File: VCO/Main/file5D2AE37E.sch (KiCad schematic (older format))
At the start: 28 parts, among them U5 LM13700, U6 TL072, U7 TL072

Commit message: Resolve most of the issues in known_issues.txt
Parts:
- R25: value 10K -> 20K
- R35: value 20K -> 10K
- R38: value 24K -> 12K
- R39: value 9.1K -> 10K
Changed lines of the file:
@@
 EESchema Schematic File Version 4
-LIBS:AS3340_VCO-cache
-EELAYER 29 0
+LIBS:VCO_Main-cache
+EELAYER 30 0
 EELAYER END
 $Descr A4 11693 8268
@@
 AR Path="/5D2AE37F/5D4E2D40" Ref="R35"  Part="1"
 F 0 "R35" V 2105 6750 50  0000 C CNN
-F 1 "20K" V 2014 6750 50  0000 C CNN
+F 1 "10K" V 2014 6750 50  0000 C CNN
 F 2 "Resistor_SMD:R_0805_2012Metric" V 1940 6740 50  0001 C CNN
 F 3 "~" H 1900 6750 50  0001 C CNN
@@
 AR Path="/5D2AE37F/5D513054" Ref="R38"  Part="1"
 F 0 "R38" V 8355 5800 50  0000 C CNN
-F 1 "24K" V 8264 5800 50  0000 C CNN
+F 1 "12K" V 8264 5800 50  0000 C CNN
 F 2 "Resistor_SMD:R_0805_2012Metric" V 8190 5790 50  0001 C CNN
 F 3 "~" H 8150 5800 50  0001 C CNN
@@
 AR Path="/5D2AE37F/5D513604" Ref="R39"  Part="1"
 F 0 "R39" V 9155 6200 50  0000 C CNN
-F 1 "9.1K" V 9064 6200 50  0000 C CNN
+F 1 "10K" V 9064 6200 50  0000 C CNN
 F 2 "Resistor_SMD:R_0805_2012Metric" V 8990 6190 50  0001 C CNN
 F 3 "~" H 8950 6200 50  0001 C CNN
@@
 AR Path="/5D2AE37F/5D551AEB" Ref="R25"  Part="1"
 F 0 "R25" V 3255 4300 50  0000 C CNN
-F 1 "10K" V 3164 4300 50  0000 C CNN
+F 1 "20K" V 3164 4300 50  0000 C CNN
 F 2 "Resistor_SMD:R_0805_2012Metric" V 3090 4290 50  0001 C CNN
 F 3 "~" H 3050 4300 50  0001 C CNN

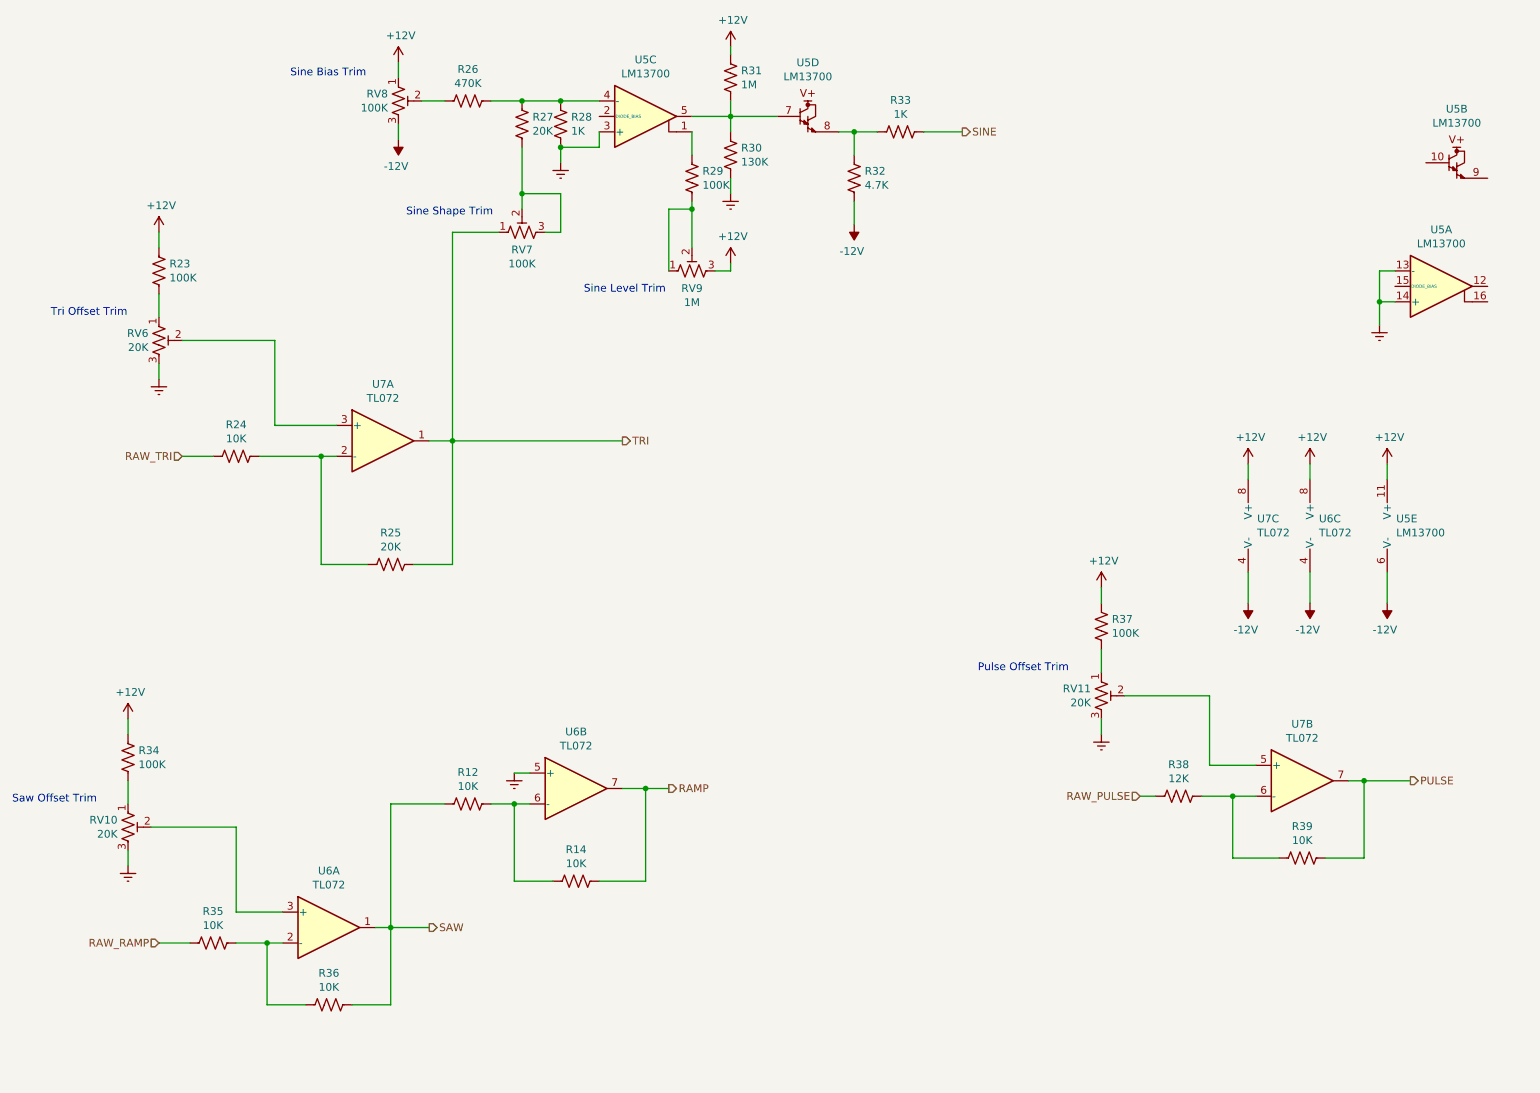
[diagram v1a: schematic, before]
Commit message: Clean up layout of VCO board
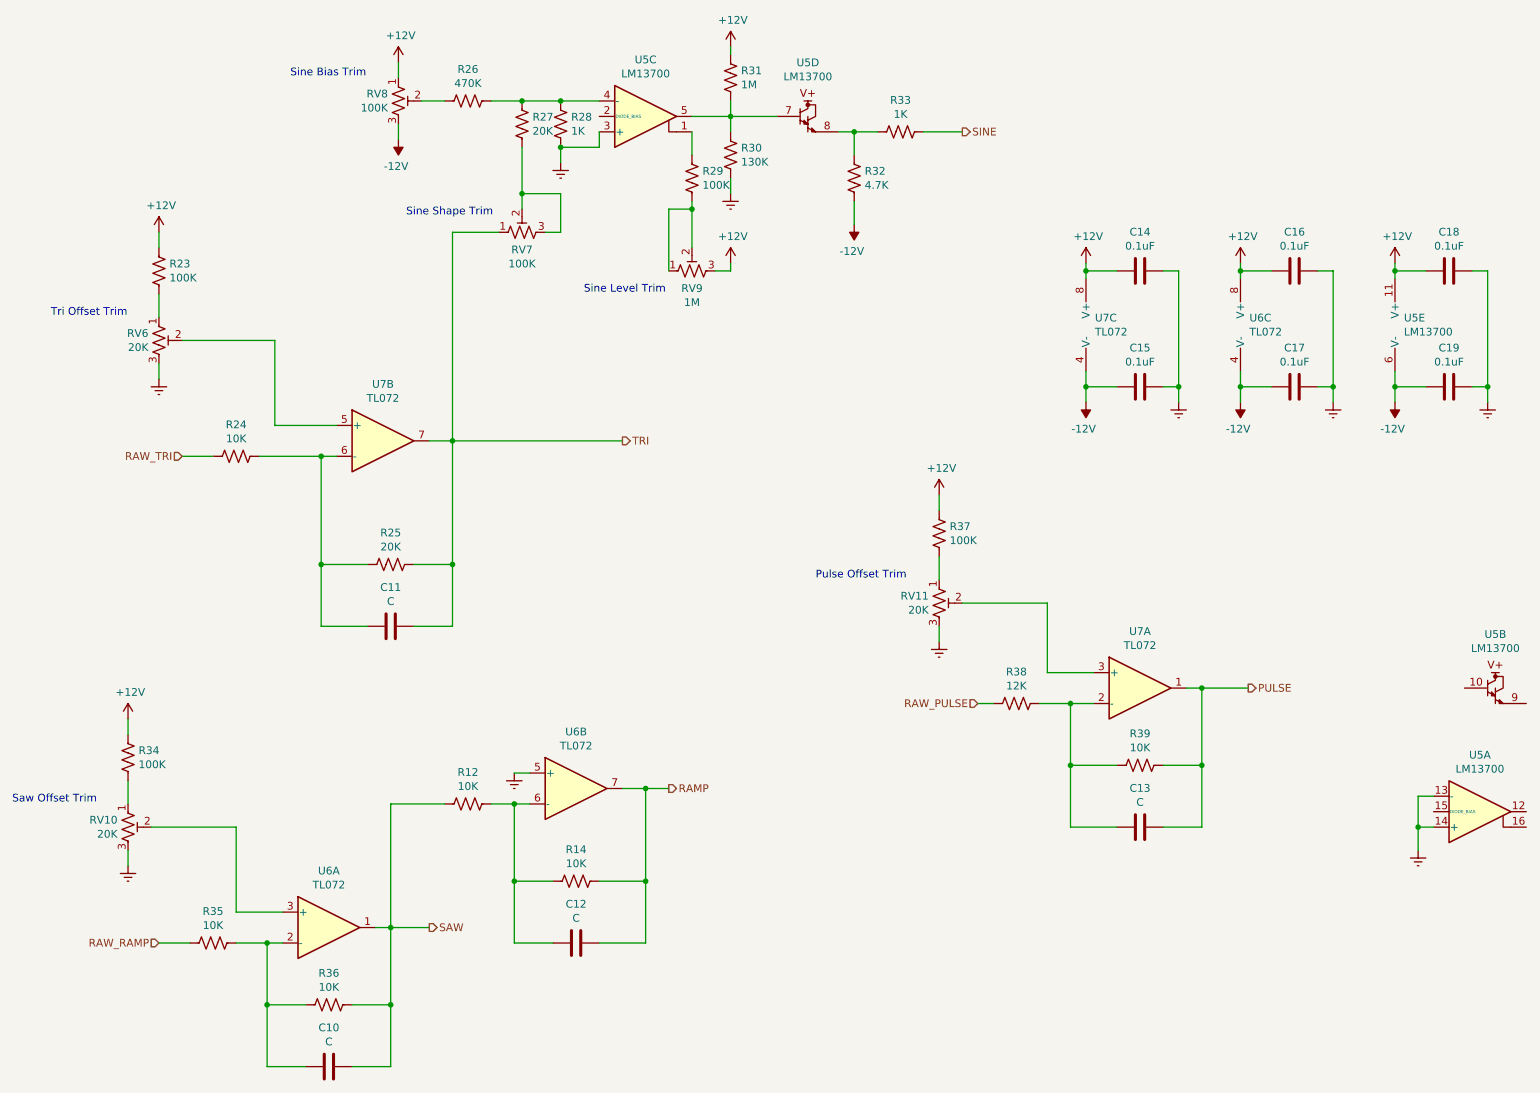
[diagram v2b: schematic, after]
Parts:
- added C10, C11, C12, C13: C, Capacitor_SMD:C_0805_2012Metric, symbol Device:C
- added C14, C15, C16, C17, C18, C19: 0.1uF, Capacitor_SMD:C_0805_2012Metric, symbol Device:C
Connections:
- net +12V: now also C14.2, C16.2, C18.2
- net -12V: now also C15.2, C17.2, C19.2
- net GNDREF: now also C14.1, C15.1, C16.1, C17.1, C18.1, C19.1
- net PULSE: now also U7.1, C13.1; no longer U7.7
- net RAMP: now also C12.1
- net SAW: now also C10.1
- net TRI: now also U7.7, C11.1; no longer U7.1
- net at R35.2, R36.1, U6.2 (-): now also C10.2
- net at R12.2, R14.1, U6.6 (-): now also C12.2
- net at R38.2, R39.1: now also U7.2 (-), C13.2; no longer U7.6 (-)
- net at RV11.2: now also U7.3 (+); no longer U7.5 (+)
- net at R24.2, R25.1: now also U7.6 (-), C11.2; no longer U7.2 (-)
- net at RV6.2: now also U7.5 (+); no longer U7.3 (+)
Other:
- moved on the sheet: R37, R38, R39, RV11, U5A, U5B, U5E, U6C, U7A, U7B, U7C
